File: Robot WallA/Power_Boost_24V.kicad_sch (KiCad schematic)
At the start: 31 parts, among them IC1 ABXS005A4X341-SRZ, Q1 BSS138, U3 125700D00000G, U4 125700D00000G

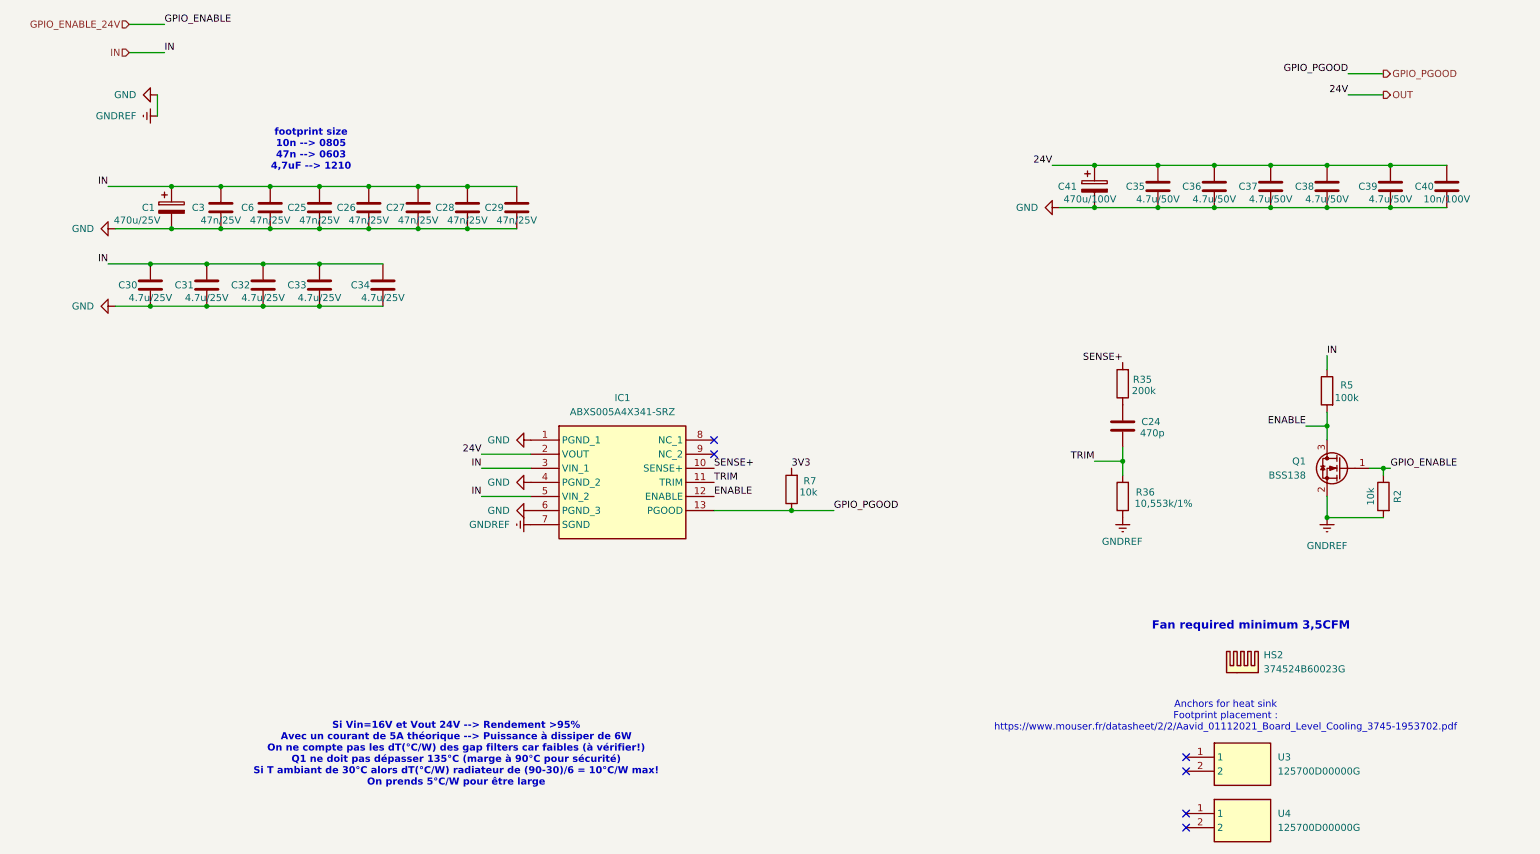
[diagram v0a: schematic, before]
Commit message: Continued to link MCU pins, Added a sheet for servomotors and optional 2 DC motors.
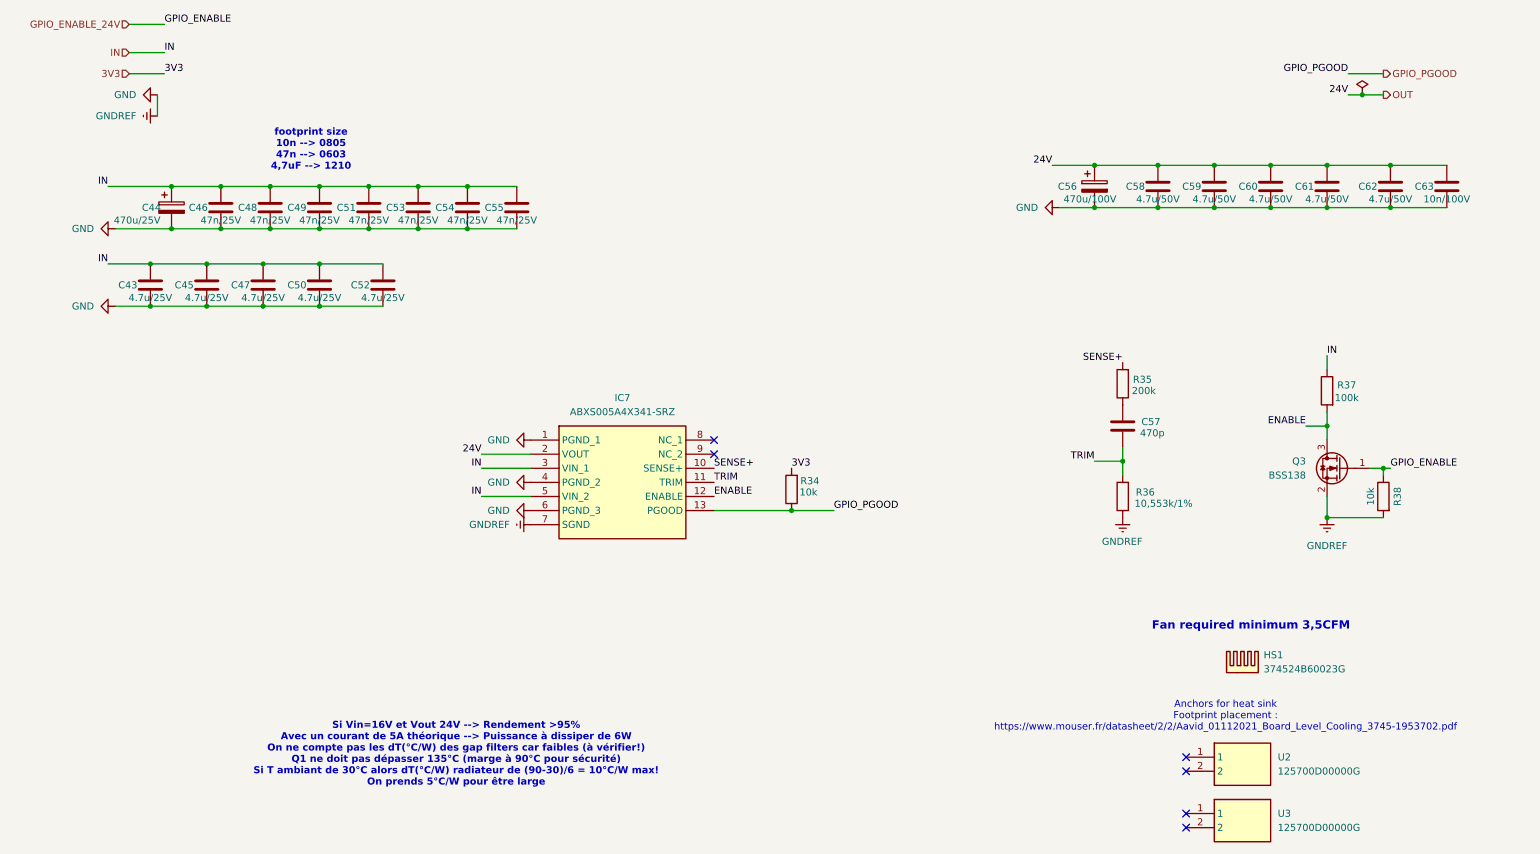
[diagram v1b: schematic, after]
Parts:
- renumbered C30 to C43, C1 to C44, C31 to C45, C3 to C46, C32 to C47, C6 to C48, C25 to C49, C33 to C50, C26 to C51, C34 to C52, C27 to C53, C28 to C54, C29 to C55, C41 to C56, C24 to C57, C35 to C58, C36 to C59, C37 to C60, C38 to C61, C39 to C62, C40 to C63, HS2 to HS1, IC1 to IC7, Q1 to Q3, R7 to R34, R5 to R37, R2 to R38, U3 to U2, U4 to U3

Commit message: Defined every footprints
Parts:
- added D13: LED_RED, LED_SMD:LED_0603_1608Metric, symbol Device:LED
- added R50: 11.1k, Resistor_SMD:R_0603_1608Metric_Pad0.98x0.95mm_HandSolder, symbol Device:R
- C62: renamed from C56; value 470u/100V -> 470uF/50V; footprint (none) -> SamacSys_Parts:CAPAE1700X1700N; Manufacturer_Part_Number (none) -> EMVE500ARA471MLH0S
- C63: renamed from C58; value 4.7u/50V -> 4.7uF/50V; footprint (none) -> Capacitor_SMD:C_0805_2012Metric_Pad1.18x1.45mm_HandSolder
- C64: renamed from C59; value 4.7u/50V -> 4.7uF/50V; footprint (none) -> Capacitor_SMD:C_0805_2012Metric_Pad1.18x1.45mm_HandSolder
- C65: renamed from C60; value 4.7u/50V -> 4.7uF/50V; footprint (none) -> Capacitor_SMD:C_0805_2012Metric_Pad1.18x1.45mm_HandSolder
- C66: renamed from C61; value 4.7u/50V -> 4.7uF/50V; footprint (none) -> Capacitor_SMD:C_0805_2012Metric_Pad1.18x1.45mm_HandSolder
- C67: renamed from C62; value 4.7u/50V -> 4.7uF/50V; footprint (none) -> Capacitor_SMD:C_0805_2012Metric_Pad1.18x1.45mm_HandSolder
- C68: renamed from C63; value 10n/100V -> 10nF/50V; footprint (none) -> Capacitor_SMD:C_0805_2012Metric_Pad1.18x1.45mm_HandSolder
- C69: renamed from C44; value 470u/25V -> 470uF/50V; footprint (none) -> SamacSys_Parts:CAPAE1700X1700N; Manufacturer_Part_Number (none) -> EMVE500ARA471MLH0S
- C70: renamed from C46; value 47n/25V -> 47nF/25V; footprint (none) -> Capacitor_SMD:C_0603_1608Metric_Pad1.08x0.95mm_HandSolder
- C71: renamed from C48; value 47n/25V -> 47nF/25V; footprint (none) -> Capacitor_SMD:C_0603_1608Metric_Pad1.08x0.95mm_HandSolder
- C72: renamed from C49; value 47n/25V -> 47nF/25V; footprint (none) -> Capacitor_SMD:C_0603_1608Metric_Pad1.08x0.95mm_HandSolder
- C73: renamed from C51; value 47n/25V -> 47nF/25V; footprint (none) -> Capacitor_SMD:C_0603_1608Metric_Pad1.08x0.95mm_HandSolder
- C74: renamed from C53; value 47n/25V -> 47nF/25V; footprint (none) -> Capacitor_SMD:C_0603_1608Metric_Pad1.08x0.95mm_HandSolder
- C75: renamed from C54; value 47n/25V -> 47nF/25V; footprint (none) -> Capacitor_SMD:C_0603_1608Metric_Pad1.08x0.95mm_HandSolder
- C76: renamed from C55; value 47n/25V -> 47nF/25V; footprint (none) -> Capacitor_SMD:C_0603_1608Metric_Pad1.08x0.95mm_HandSolder
- C77: renamed from C43; value 4.7u/25V -> 4.7uF/25V; footprint (none) -> Capacitor_SMD:C_1210_3225Metric_Pad1.33x2.70mm_HandSolder
- C78: renamed from C45; value 4.7u/25V -> 4.7uF/25V; footprint (none) -> Capacitor_SMD:C_1210_3225Metric_Pad1.33x2.70mm_HandSolder
- C79: renamed from C47; value 4.7u/25V -> 4.7uF/25V; footprint (none) -> Capacitor_SMD:C_1210_3225Metric_Pad1.33x2.70mm_HandSolder
- C80: renamed from C50; value 4.7u/25V -> 4.7uF/25V; footprint (none) -> Capacitor_SMD:C_1210_3225Metric_Pad1.33x2.70mm_HandSolder
- C81: renamed from C52; value 4.7u/25V -> 4.7uF/25V; footprint (none) -> Capacitor_SMD:C_1210_3225Metric_Pad1.33x2.70mm_HandSolder
- C82: renamed from C57; value 470p -> 470pF; footprint (none) -> Capacitor_SMD:C_0603_1608Metric_Pad1.08x0.95mm_HandSolder
- IC7: footprint ABXS005A4X341SRZ -> SamacSys_Parts:ABXS005A4X341SRZ; Height 8.5 -> (none); Manufacturer_Name OmniOn Power -> (none); Mouser Part Number 894-ABXS005A4X341SRZ -> (none); Mouser Price/Stock https://www.mouser.co.uk/ProductDetail/OmniOn-Power/ABXS005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 -> (none)
- R32: renamed from R35; footprint (none) -> Resistor_SMD:R_0603_1608Metric_Pad0.98x0.95mm_HandSolder
- R33: renamed from R37; footprint (none) -> Resistor_SMD:R_0603_1608Metric_Pad0.98x0.95mm_HandSolder
- R34: footprint (none) -> Resistor_SMD:R_0603_1608Metric_Pad0.98x0.95mm_HandSolder
- R35: renamed from R36; footprint (none) -> Resistor_SMD:R_0603_1608Metric_Pad0.98x0.95mm_HandSolder
- R36: renamed from R38; footprint (none) -> Resistor_SMD:R_0603_1608Metric_Pad0.98x0.95mm_HandSolder
- U2, U3: footprint 125700D00000G -> SamacSys_Parts:125700D00000G; Arrow Part Number 125700D00000G -> (none); Arrow Price/Stock https://www.arrow.com/en/products/125700d00000g/aavid-therm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 -> (none); Height 7.19 -> (none); Manufacturer_Name Aavid Thermalloy -> (none); Mouser Part Number 532-125700D00000G -> (none); Mouser Price/Stock https://www.mouser.co.uk/ProductDetail/Aavid/125700D00000G?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 -> (none)
- renumbered Q3 to Q2
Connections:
- net GND: now also R50.2
- net OUT: now also D13.2 (A)
- new net: D13.1 (K), R50.1

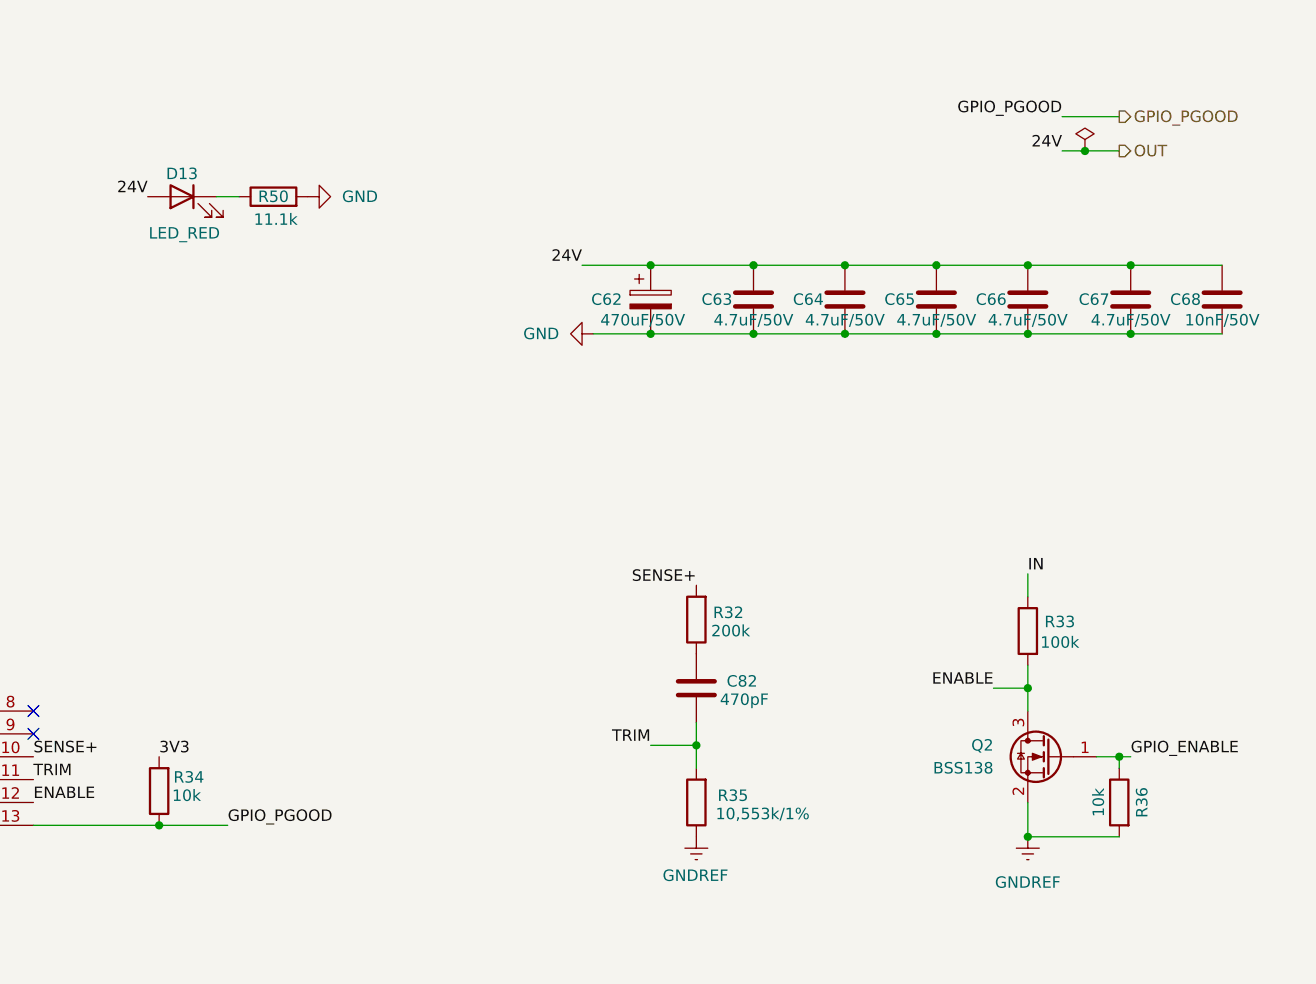
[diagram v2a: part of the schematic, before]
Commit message: Updated USB UART converter, Linked telemeter sensors.
Updated components indicators
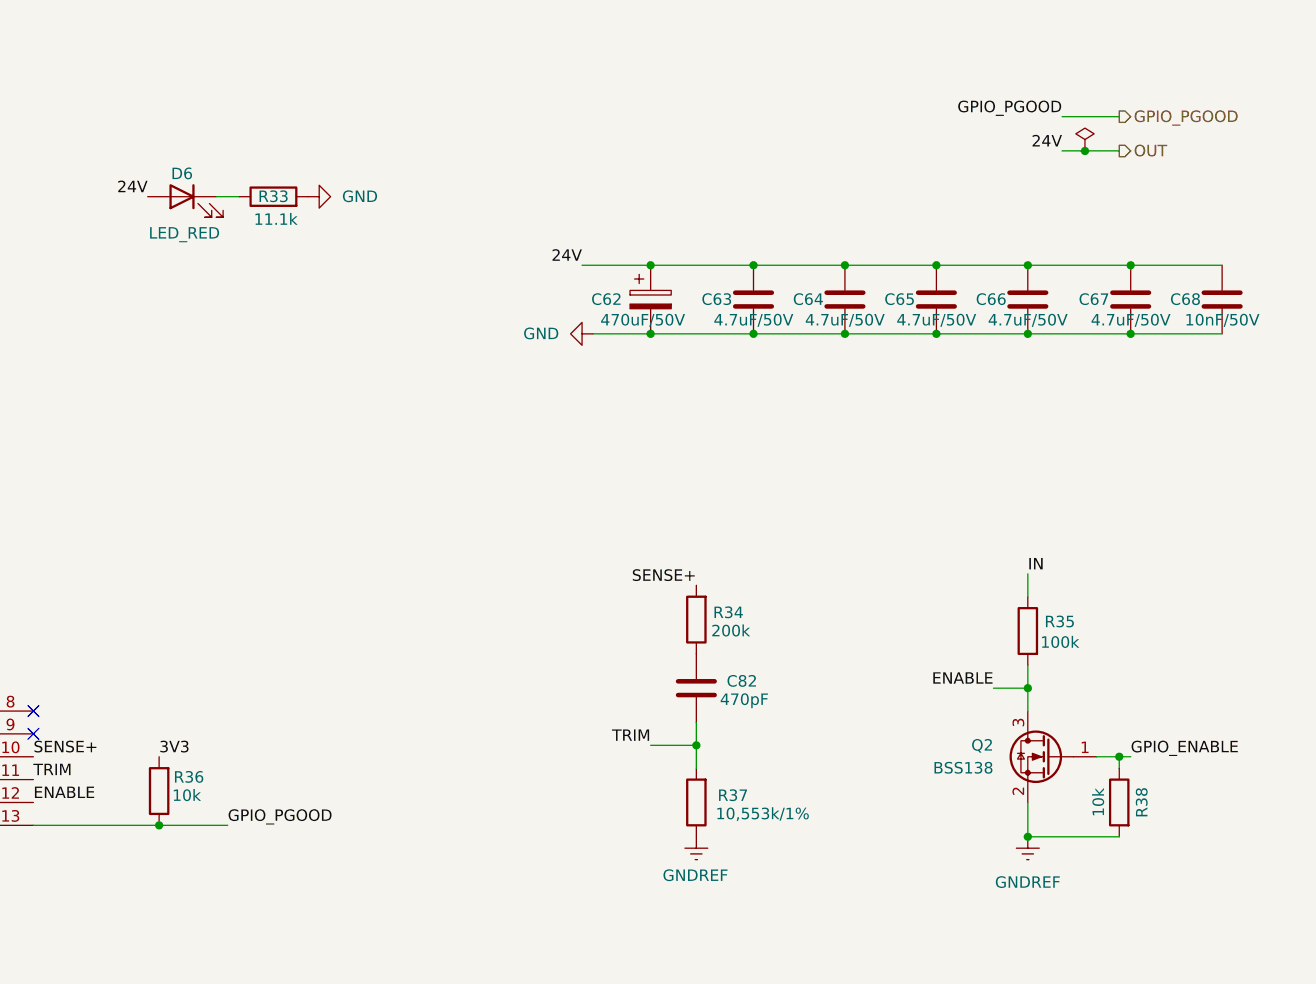
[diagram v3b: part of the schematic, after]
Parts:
- Q2: Manufacturer_Part_Number (none) -> BSS138
- renumbered D13 to D6, R50 to R33, R32 to R34, R33 to R35, R34 to R36, R35 to R37, R36 to R38
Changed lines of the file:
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@@
 		(dnp no)
 		(fields_autoplaced yes)
-		(property "Reference" "#PWR067"
+		(property "Reference" "#PWR071"
 			(at 191.77 50.8 0)
 			(effects
@@
 			(project "PCB"
 				(path "/117fd49e-499d-4b54-b58c-f6b538ecca4a/d5f4dab0-e2de-4083-971d-4b1eb9c8d4bb/f849c0a2-f150-4f7d-9c03-1f3f5fdefafe"
-					(reference "#PWR067")
+					(reference "#PWR071")
 					(unit 1)
 				)
@@
 		(dnp no)
 		(fields_autoplaced yes)
-		(property "Reference" "#PWR066"
+		(property "Reference" "#PWR069"
 			(at 29.21 34.29 0)
 			(effects
@@
 			(project "PCB"
 				(path "/117fd49e-499d-4b54-b58c-f6b538ecca4a/d5f4dab0-e2de-4083-971d-4b1eb9c8d4bb/f849c0a2-f150-4f7d-9c03-1f3f5fdefafe"
-					(reference "#PWR066")
+					(reference "#PWR069")
 					(unit 1)
 				)
@@
 		(dnp no)
 		(fields_autoplaced yes)
-		(property "Reference" "#PWR075"
+		(property "Reference" "#PWR079"
 			(at 96.52 107.95 0)
 			(effects
@@
 			(project "PCB"
 				(path "/117fd49e-499d-4b54-b58c-f6b538ecca4a/d5f4dab0-e2de-4083-971d-4b1eb9c8d4bb/f849c0a2-f150-4f7d-9c03-1f3f5fdefafe"
-					(reference "#PWR075")
+					(reference "#PWR079")
 					(unit 1)
 				)
@@
 		(on_board yes)
 		(dnp no)
-		(property "Reference" "R33"
+		(property "Reference" "R35"
 			(at 249.936 82.804 0)
 			(effects
@@
 			(project "PCB"
 				(path "/117fd49e-499d-4b54-b58c-f6b538ecca4a/d5f4dab0-e2de-4083-971d-4b1eb9c8d4bb/f849c0a2-f150-4f7d-9c03-1f3f5fdefafe"
-					(reference "R33")
+					(reference "R35")
 					(unit 1)
 				)
@@
 		(dnp no)
 		(fields_autoplaced yes)
-		(property "Reference" "#PWR070"
+		(property "Reference" "#PWR074"
 			(at 96.52 92.71 0)
 			(effects
@@
 			(project "PCB"
 				(path "/117fd49e-499d-4b54-b58c-f6b538ecca4a/d5f4dab0-e2de-4083-971d-4b1eb9c8d4bb/f849c0a2-f150-4f7d-9c03-1f3f5fdefafe"
-					(reference "#PWR070")
+					(reference "#PWR074")
 					(unit 1)
 				)
@@
 		(on_board yes)
 		(dnp no)
-		(property "Reference" "R34"
+		(property "Reference" "R36"
 			(at 153.162 100.076 0)
 			(effects
@@
 			(project "PCB"
 				(path "/117fd49e-499d-4b54-b58c-f6b538ecca4a/d5f4dab0-e2de-4083-971d-4b1eb9c8d4bb/f849c0a2-f150-4f7d-9c03-1f3f5fdefafe"
-					(reference "R34")
+					(reference "R36")
 					(unit 1)
 				)
@@
 		(dnp no)
 		(fields_autoplaced yes)
-		(property "Reference" "#PWR074"
+		(property "Reference" "#PWR078"
 			(at 246.38 113.03 0)
 			(effects
@@
 			(project "PCB"
 				(path "/117fd49e-499d-4b54-b58c-f6b538ecca4a/d5f4dab0-e2de-4083-971d-4b1eb9c8d4bb/f849c0a2-f150-4f7d-9c03-1f3f5fdefafe"
-					(reference "#PWR074")
+					(reference "#PWR078")
 					(unit 1)
 				)
@@
 		(dnp no)
 		(fields_autoplaced yes)
-		(property "Reference" "#PWR071"
+		(property "Reference" "#PWR075"
 			(at 96.52 100.33 0)
 			(effects
@@
 			(project "PCB"
 				(path "/117fd49e-499d-4b54-b58c-f6b538ecca4a/d5f4dab0-e2de-4083-971d-4b1eb9c8d4bb/f849c0a2-f150-4f7d-9c03-1f3f5fdefafe"
-					(reference "#PWR071")
+					(reference "#PWR075")
 					(unit 1)
 				)
@@
 		(on_board yes)
 		(dnp no)
-		(property "Reference" "R50"
+		(property "Reference" "R33"
 			(at 162.56 35.56 90)
 			(effects
@@
 			(project "Robot WallA"
 				(path "/117fd49e-499d-4b54-b58c-f6b538ecca4a/d5f4dab0-e2de-4083-971d-4b1eb9c8d4bb/f849c0a2-f150-4f7d-9c03-1f3f5fdefafe"
-					(reference "R50")
+					(reference "R33")
 					(unit 1)
 				)
@@
 		(dnp no)
 		(fields_autoplaced yes)
-		(property "Reference" "#PWR0123"
+		(property "Reference" "#PWR070"
 			(at 172.72 35.56 0)
 			(effects
@@
 			(project "Robot WallA"
 				(path "/117fd49e-499d-4b54-b58c-f6b538ecca4a/d5f4dab0-e2de-4083-971d-4b1eb9c8d4bb/f849c0a2-f150-4f7d-9c03-1f3f5fdefafe"
-					(reference "#PWR0123")
+					(reference "#PWR070")
 					(unit 1)
 				)
@@
 		(dnp no)
 		(fields_autoplaced yes)
-		(property "Reference" "#PWR068"
+		(property "Reference" "#PWR072"
 			(at 21.59 54.61 0)
 			(effects
@@
 			(project "PCB"
 				(path "/117fd49e-499d-4b54-b58c-f6b538ecca4a/d5f4dab0-e2de-4083-971d-4b1eb9c8d4bb/f849c0a2-f150-4f7d-9c03-1f3f5fdefafe"
-					(reference "#PWR068")
+					(reference "#PWR072")
 					(unit 1)
 				)
@@
 		(on_board yes)
 		(dnp no)
-		(property "Reference" "R36"
+		(property "Reference" "R38"
 			(at 259.08 102.87 90)
 			(effects
@@
 			(project "PCB"
 				(path "/117fd49e-499d-4b54-b58c-f6b538ecca4a/d5f4dab0-e2de-4083-971d-4b1eb9c8d4bb/f849c0a2-f150-4f7d-9c03-1f3f5fdefafe"
-					(reference "R36")
+					(reference "R38")
 					(unit 1)
 				)
@@
 		(on_board yes)
 		(dnp no)
-		(property "Reference" "R32"
+		(property "Reference" "R34"
 			(at 213.106 81.788 0)
 			(effects
@@
 			(project "PCB"
 				(path "/117fd49e-499d-4b54-b58c-f6b538ecca4a/d5f4dab0-e2de-4083-971d-4b1eb9c8d4bb/f849c0a2-f150-4f7d-9c03-1f3f5fdefafe"
-					(reference "R32")
+					(reference "R34")
 					(unit 1)
 				)
@@
 		(on_board yes)
 		(dnp no)
-		(property "Reference" "D13"
+		(property "Reference" "D6"
 			(at 152.4 33.02 0)
 			(effects
@@
 			(project "Robot WallA"
 				(path "/117fd49e-499d-4b54-b58c-f6b538ecca4a/d5f4dab0-e2de-4083-971d-4b1eb9c8d4bb/f849c0a2-f150-4f7d-9c03-1f3f5fdefafe"
-					(reference "D13")
+					(reference "D6")
 					(unit 1)
 				)
@@
 		(dnp no)
 		(fields_autoplaced yes)
-		(property "Reference" "#PWR072"
+		(property "Reference" "#PWR076"
 			(at 96.52 105.41 0)
 			(effects
@@
 			(project "PCB"
 				(path "/117fd49e-499d-4b54-b58c-f6b538ecca4a/d5f4dab0-e2de-4083-971d-4b1eb9c8d4bb/f849c0a2-f150-4f7d-9c03-1f3f5fdefafe"
-					(reference "#PWR072")
+					(reference "#PWR076")
 					(unit 1)
 				)
@@
 		(dnp no)
 		(fields_autoplaced yes)
-		(property "Reference" "#PWR065"
+		(property "Reference" "#PWR068"
 			(at 29.21 30.48 0)
 			(effects
@@
 			(project "PCB"
 				(path "/117fd49e-499d-4b54-b58c-f6b538ecca4a/d5f4dab0-e2de-4083-971d-4b1eb9c8d4bb/f849c0a2-f150-4f7d-9c03-1f3f5fdefafe"
-					(reference "#PWR065")
+					(reference "#PWR068")
 					(unit 1)
 				)
@@
 		(on_board yes)
 		(dnp no)
-		(property "Reference" "R35"
+		(property "Reference" "R37"
 			(at 213.614 102.108 0)
 			(effects
@@
 			(project "PCB"
 				(path "/117fd49e-499d-4b54-b58c-f6b538ecca4a/d5f4dab0-e2de-4083-971d-4b1eb9c8d4bb/f849c0a2-f150-4f7d-9c03-1f3f5fdefafe"
-					(reference "R35")
+					(reference "R37")
 					(unit 1)
 				)
@@
 		(on_board yes)
 		(dnp no)
-		(property "Reference" "#PWR073"
+		(property "Reference" "#PWR077"
 			(at 209.55 113.03 0)
 			(effects
@@
 			(project "PCB"
 				(path "/117fd49e-499d-4b54-b58c-f6b538ecca4a/d5f4dab0-e2de-4083-971d-4b1eb9c8d4bb/f849c0a2-f150-4f7d-9c03-1f3f5fdefafe"
-					(reference "#PWR073")
+					(reference "#PWR077")
 					(unit 1)
 				)
@@
 		(dnp no)
 		(fields_autoplaced yes)
-		(property "Reference" "#PWR069"
+		(property "Reference" "#PWR073"
 			(at 21.59 68.58 0)
 			(effects
@@
 			(project "PCB"
 				(path "/117fd49e-499d-4b54-b58c-f6b538ecca4a/d5f4dab0-e2de-4083-971d-4b1eb9c8d4bb/f849c0a2-f150-4f7d-9c03-1f3f5fdefafe"
-					(reference "#PWR069")
+					(reference "#PWR073")
 					(unit 1)
 				)
@@
 			(at 248.92 97.79 0)
 			(effects
+				(font
+					(size 1.27 1.27)
+				)
+				(hide yes)
+			)
+		)
+		(property "Manufacturer_Part_Number" "BSS138"
+			(at 248.92 97.79 0)
+			(effects
